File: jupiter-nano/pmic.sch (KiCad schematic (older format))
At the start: 51 parts, among them Q1 BSS138, Q2 BSS138, Q3 BSS138, Q4 BSS138, Q5 BSS138, U2 ACT8945AQJ305-T

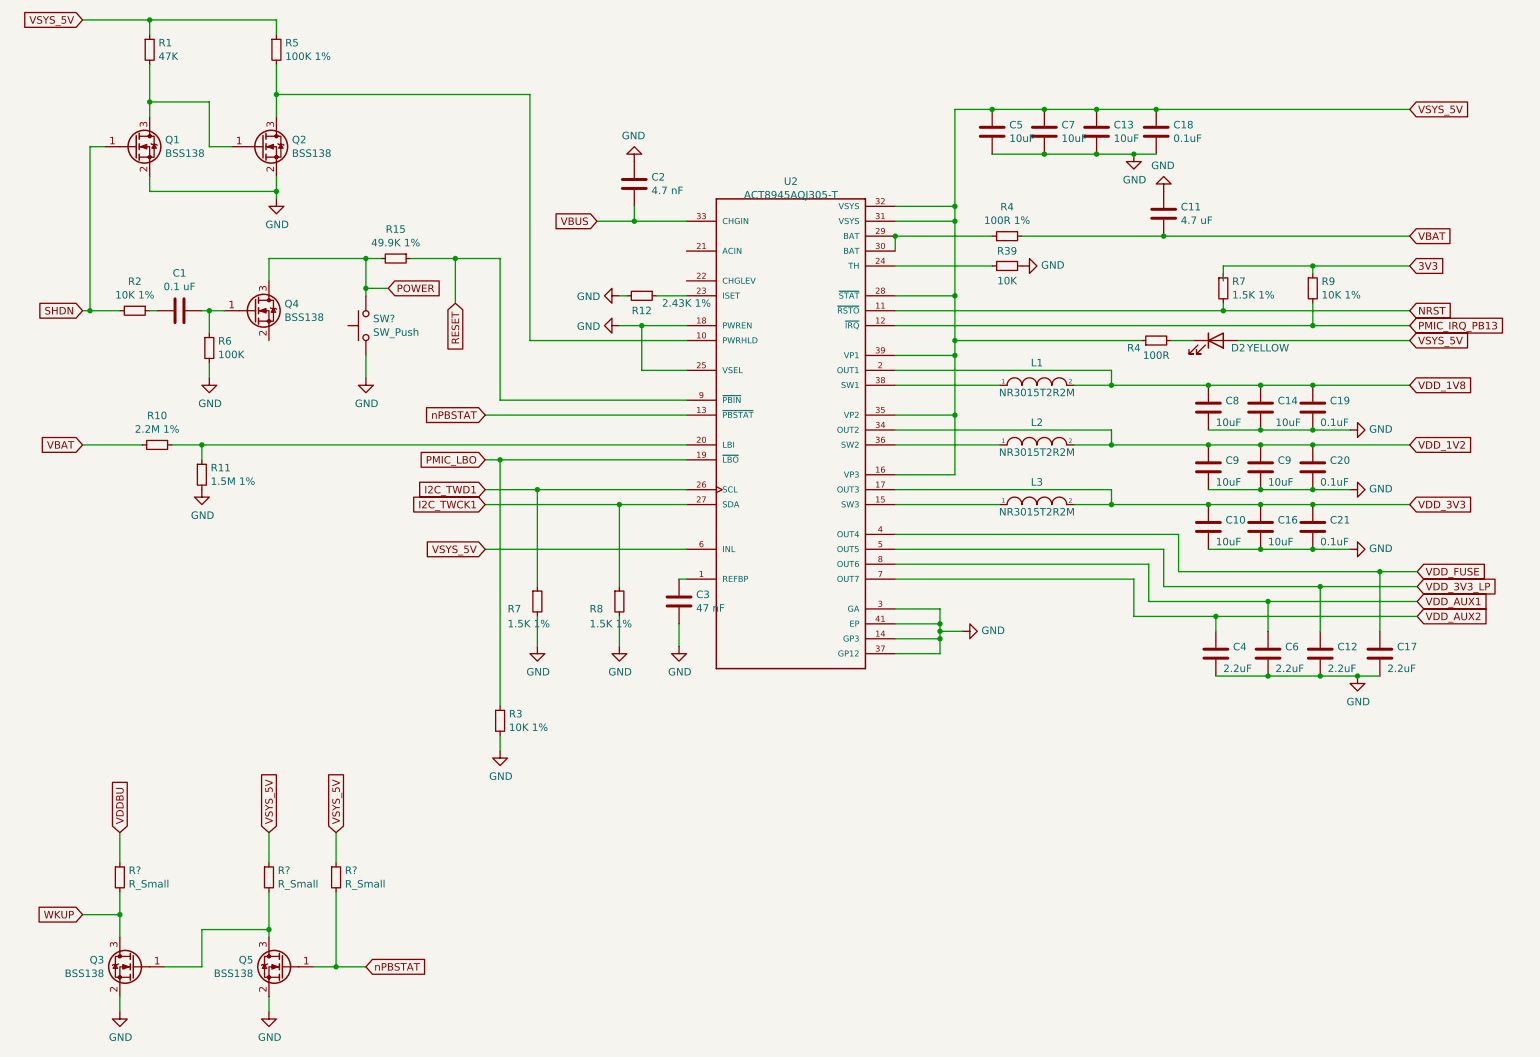
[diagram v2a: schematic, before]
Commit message: fixed error with INL
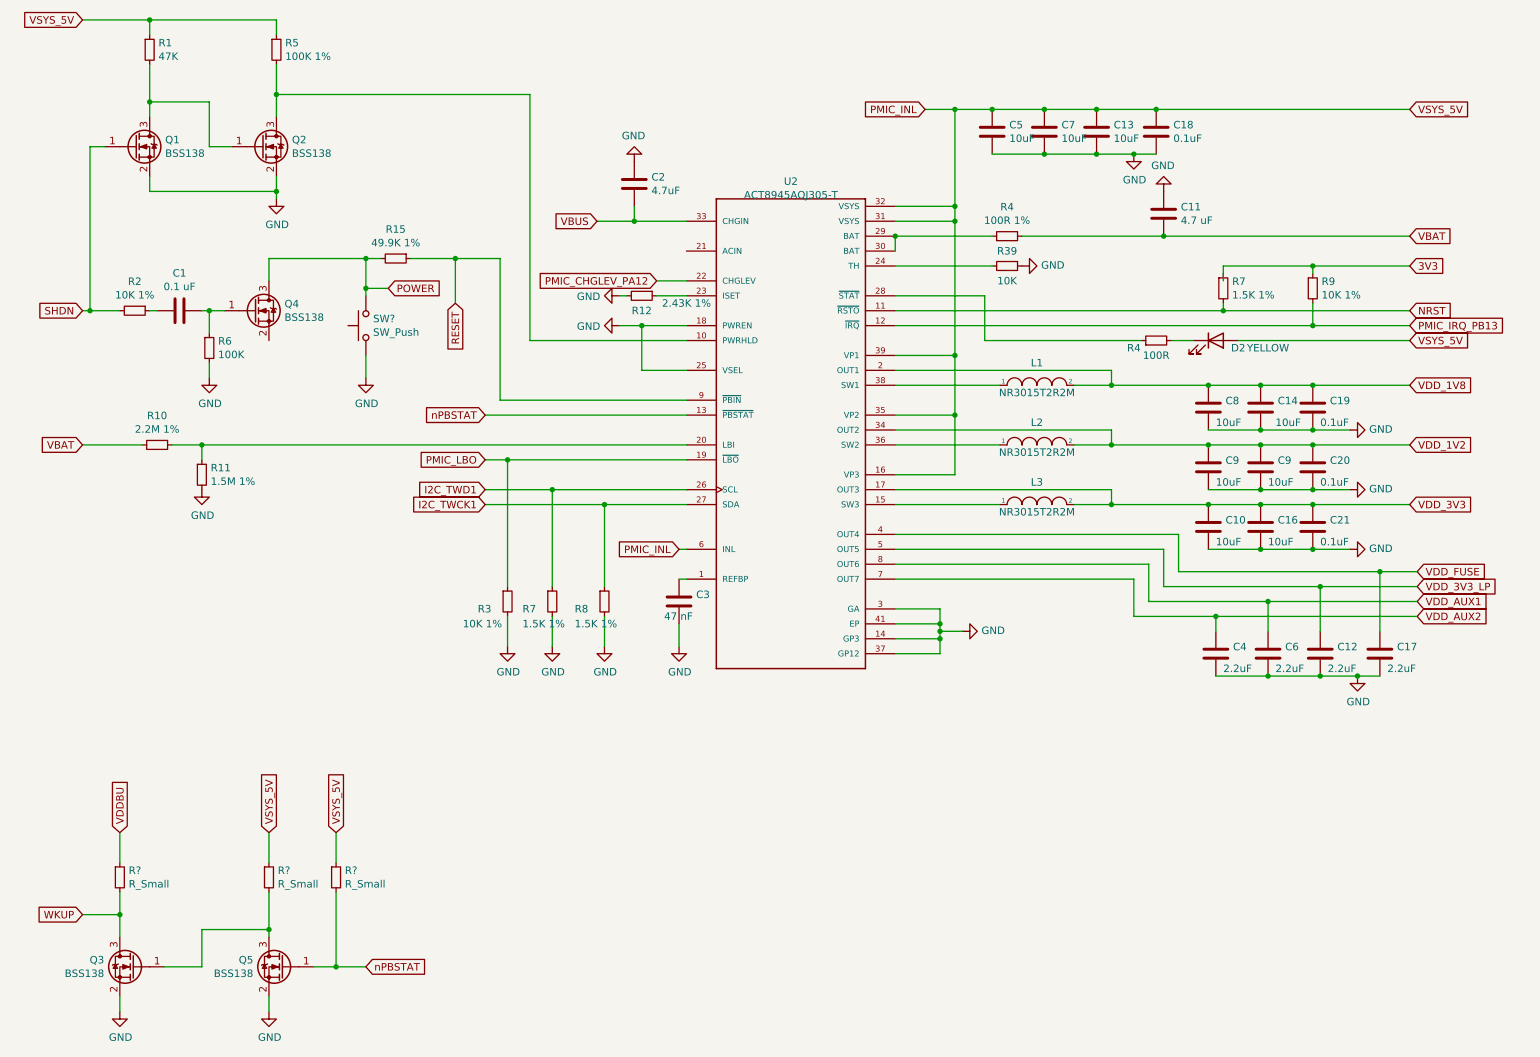
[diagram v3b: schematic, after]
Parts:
- C2: value 4.7 nF -> 4.7uF
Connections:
- net PMIC_CHGLEV_PA12: now reaches U2.22 (CHGLEV)
- net VSYS_5V renamed PMIC_INL
- net PMIC_INL: no longer R4.1, U2.28 (~STAT~)
- new net: R4.1, U2.28 (~STAT~)
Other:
- moved on the sheet: R3, R7, R8
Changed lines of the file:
@@
 P 4650 1900
 F 0 "C2" H 4765 1946 50  0000 L CNN
-F 1 "4.7 nF" H 4765 1855 50  0000 L CNN
+F 1 "4.7uF" H 4765 1855 50  0000 L CNN
 F 2 "Capacitor_SMD:C_0201_0603Metric" H 4688 1750 50  0001 C CNN
 F 3 "~" H 4650 1900 50  0001 C CNN
@@
 $EndComp
 Wire Wire Line
-	5000 3750 3750 3750
+	5000 3750 3800 3750
 Text GLabel 3650 3750 0    50   Input ~ 0
 PMIC_LBO
@@
 Text GLabel 9850 1400 2    50   Input ~ 0
 VSYS_5V
-Wire Wire Line
-	5000 4350 3650 4350
-Text GLabel 3650 4350 0    50   Input ~ 0
-VSYS_5V
+Text GLabel 4950 4350 0    50   Input ~ 0
+PMIC_INL
 $Comp
 L Device:C C5
@@
 $EndComp
 Wire Wire Line
-	6400 2650 6800 2650
-Wire Wire Line
-	6800 2650 6800 2150
-Wire Wire Line
 	6400 2450 7050 2450
 $Comp
@@
 Wire Wire Line
 	6800 3450 6800 3050
-Connection ~ 6800 2650
 Connection ~ 6800 3050
 Wire Wire Line
-	6800 3050 6800 2950
-Wire Wire Line
 	6400 3050 6800 3050
-Connection ~ 6800 2950
-Wire Wire Line
-	6800 2950 6800 2650
 Connection ~ 8200 2250
 Wire Wire Line
@@
 	8700 2950 9850 2950
 Wire Wire Line
-	6800 2950 8050 2950
-Wire Wire Line
 	6400 4750 6700 4750
 Wire Wire Line
@@
 P 4950 4700
 F 0 "C3" H 5065 4746 50  0000 L CNN
-F 1 "47 nF" H 5065 4655 50  0000 L CNN
+F 1 "47 nF" H 4850 4600 50  0000 L CNN
 F 2 "Capacitor_SMD:C_0201_0603Metric" H 4988 4550 50  0001 C CNN
 F 3 "~" H 4950 4700 50  0001 C CNN
@@
 nPBSTAT
 Wire Wire Line
-	5000 3950 4000 3950
-Text GLabel 3650 3950 0    50   Input ~ 0
-I2C_TWD1
-Wire Wire Line
-	5000 4050 4550 4050
+	5000 3950 4100 3950
+Wire Wire Line
+	5000 4050 4450 4050
 Text GLabel 3650 4050 0    50   Input ~ 0
 I2C_TWCK1
 Wire Wire Line
-	4000 3950 4000 4600
-Connection ~ 4000 3950
-Wire Wire Line
-	4000 3950 3650 3950
-Wire Wire Line
-	4550 4050 4550 4600
-Connection ~ 4550 4050
-Wire Wire Line
-	4550 4050 3650 4050
+	4100 3950 4100 4600
+Connection ~ 4100 3950
+Wire Wire Line
+	4100 3950 3650 3950
+Wire Wire Line
+	4450 4050 4450 4600
+Connection ~ 4450 4050
+Wire Wire Line
+	4450 4050 3650 4050
 $Comp
 L Device:R_Small R7
 U 1 1 5F5D8A0F
-P 4000 4700
-F 0 "R7" H 3800 4650 50  0000 L CNN
-F 1 "1.5K 1%" H 3800 4550 50  0000 L CNN
-F 2 "Capacitor_SMD:C_0201_0603Metric" H 4000 4700 50  0001 C CNN
-F 3 "~" H 4000 4700 50  0001 C CNN
-	1    4000 4700
+P 4100 4700
+F 0 "R7" H 3900 4650 50  0000 L CNN
+F 1 "1.5K 1%" H 3900 4550 50  0000 L CNN
+F 2 "Capacitor_SMD:C_0201_0603Metric" H 4100 4700 50  0001 C CNN
+F 3 "~" H 4100 4700 50  0001 C CNN
+	1    4100 4700
 	1    0    0    -1
 $EndComp
@@
 L Device:R_Small R8
 U 1 1 5F5D9763
-P 4550 4700
-F 0 "R8" H 4350 4650 50  0000 L CNN
-F 1 "1.5K 1%" H 4350 4550 50  0000 L CNN
-F 2 "Capacitor_SMD:C_0201_0603Metric" H 4550 4700 50  0001 C CNN
-F 3 "~" H 4550 4700 50  0001 C CNN
-	1    4550 4700
-	1    0    0    -1
-$EndComp
-Wire Wire Line
-	4000 4800 4000 5000
-Wire Wire Line
-	4550 4800 4550 5000
+P 4450 4700
+F 0 "R8" H 4250 4650 50  0000 L CNN
+F 1 "1.5K 1%" H 4250 4550 50  0000 L CNN
+F 2 "Capacitor_SMD:C_0201_0603Metric" H 4450 4700 50  0001 C CNN
+F 3 "~" H 4450 4700 50  0001 C CNN
+	1    4450 4700
+	1    0    0    -1
+$EndComp
+Wire Wire Line
+	4100 4800 4100 5000
+Wire Wire Line
+	4450 4800 4450 5000
 $Comp
 L power:GND #PWR?
 U 1 1 5F5E58C5
-P 4000 5000
-F 0 "#PWR?" H 4000 4750 50  0001 C CNN
-F 1 "GND" H 4005 4827 50  0000 C CNN
-F 2 "" H 4000 5000 50  0001 C CNN
-F 3 "" H 4000 5000 50  0001 C CNN
-	1    4000 5000
+P 4100 5000
+F 0 "#PWR?" H 4100 4750 50  0001 C CNN
+F 1 "GND" H 4105 4827 50  0000 C CNN
+F 2 "" H 4100 5000 50  0001 C CNN
+F 3 "" H 4100 5000 50  0001 C CNN
+	1    4100 5000
 	1    0    0    -1
 $EndComp
@@
 L power:GND #PWR?
 U 1 1 5F5E6EDB
-P 4550 5000
-F 0 "#PWR?" H 4550 4750 50  0001 C CNN
-F 1 "GND" H 4555 4827 50  0000 C CNN
-F 2 "" H 4550 5000 50  0001 C CNN
-F 3 "" H 4550 5000 50  0001 C CNN
-	1    4550 5000
-	1    0    0    -1
-$EndComp
-Wire Wire Line
-	3750 3750 3750 5400
-Connection ~ 3750 3750
-Wire Wire Line
-	3750 3750 3650 3750
+P 4450 5000
+F 0 "#PWR?" H 4450 4750 50  0001 C CNN
+F 1 "GND" H 4455 4827 50  0000 C CNN
+F 2 "" H 4450 5000 50  0001 C CNN
+F 3 "" H 4450 5000 50  0001 C CNN
+	1    4450 5000
+	1    0    0    -1
+$EndComp
+Wire Wire Line
+	3800 3750 3800 4600
+Connection ~ 3800 3750
+Wire Wire Line
+	3800 3750 3650 3750
 $Comp
 L Device:R_Small R3
 U 1 1 5F6066C1
-P 3750 5500
-F 0 "R3" H 3809 5546 50  0000 L CNN
-F 1 "10K 1%" H 3809 5455 50  0000 L CNN
-F 2 "" H 3750 5500 50  0001 C CNN
-F 3 "~" H 3750 5500 50  0001 C CNN
-	1    3750 5500
-	1    0    0    -1
-$EndComp
-Wire Wire Line
-	3750 5600 3750 5700
+P 3800 4700
+F 0 "R3" H 3600 4650 50  0000 L CNN
+F 1 "10K 1%" H 3500 4550 50  0000 L CNN
+F 2 "" H 3800 4700 50  0001 C CNN
+F 3 "~" H 3800 4700 50  0001 C CNN
+	1    3800 4700
+	1    0    0    -1
+$EndComp
+Wire Wire Line
+	3800 4800 3800 5000
 $Comp
 L power:GND #PWR?
 U 1 1 5F60CEF0
-P 3750 5700
-F 0 "#PWR?" H 3750 5450 50  0001 C CNN
-F 1 "GND" H 3755 5527 50  0000 C CNN
-F 2 "" H 3750 5700 50  0001 C CNN
-F 3 "" H 3750 5700 50  0001 C CNN
-	1    3750 5700
+P 3800 5000
+F 0 "#PWR?" H 3800 4750 50  0001 C CNN
+F 1 "GND" H 3805 4827 50  0000 C CNN
+F 2 "" H 3800 5000 50  0001 C CNN
+F 3 "" H 3800 5000 50  0001 C CNN
+	1    3800 5000
 	1    0    0    -1
 $EndComp
@@
 Wire Wire Line
 	2250 1300 3950 1300
+Wire Wire Line
+	6800 2150 6800 3050
+Wire Wire Line
+	6400 2650 7000 2650
+Wire Wire Line
+	7000 2650 7000 2950
+Wire Wire Line
+	7000 2950 8050 2950
+Wire Wire Line
+	5000 2550 4800 2550
+Text GLabel 4800 2550 0    50   Input ~ 0
+PMIC_CHGLEV_PA12
+Wire Wire Line
+	5000 4350 4950 4350
+Wire Wire Line
+	6800 1400 6600 1400
+Connection ~ 6800 1400
+Text GLabel 6600 1400 0    50   Input ~ 0
+PMIC_INL
+Text GLabel 3650 3950 0    50   Input ~ 0
+I2C_TWD1
 $EndSCHEMATC

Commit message: WIP clocking done
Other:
- moved on the sheet: Q3, Q5, R?
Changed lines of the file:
@@
 L Transistor_FET:BSS138 Q3
 U 1 1 5F66BE91
-P 1300 7150
-F 0 "Q3" H 1505 7196 50  0000 L CNN
-F 1 "BSS138" H 1505 7105 50  0000 L CNN
-F 2 "Package_TO_SOT_SMD:SOT-23" H 1500 7075 50  0001 L CIN
-F 3 "https://www.fairchildsemi.com/datasheets/BS/BSS138.pdf" H 1300 7150 50  0001 L CNN
-	1    1300 7150
+P 2300 6900
+F 0 "Q3" H 2505 6946 50  0000 L CNN
+F 1 "BSS138" H 2505 6855 50  0000 L CNN
+F 2 "Package_TO_SOT_SMD:SOT-23" H 2500 6825 50  0001 L CIN
+F 3 "https://www.fairchildsemi.com/datasheets/BS/BSS138.pdf" H 2300 6900 50  0001 L CNN
+	1    2300 6900
 	-1   0    0    -1
 $EndComp
@@
 L Transistor_FET:BSS138 Q5
 U 1 1 5F684C12
-P 2300 7150
-F 0 "Q5" H 2505 7196 50  0000 L CNN
-F 1 "BSS138" H 2505 7105 50  0000 L CNN
-F 2 "Package_TO_SOT_SMD:SOT-23" H 2500 7075 50  0001 L CIN
-F 3 "https://www.fairchildsemi.com/datasheets/BS/BSS138.pdf" H 2300 7150 50  0001 L CNN
-	1    2300 7150
+P 3300 6900
+F 0 "Q5" H 3505 6946 50  0000 L CNN
+F 1 "BSS138" H 3505 6855 50  0000 L CNN
+F 2 "Package_TO_SOT_SMD:SOT-23" H 3500 6825 50  0001 L CIN
+F 3 "https://www.fairchildsemi.com/datasheets/BS/BSS138.pdf" H 3300 6900 50  0001 L CNN
+	1    3300 6900
 	-1   0    0    -1
 $EndComp
 Wire Wire Line
-	2200 6950 2200 6900
+	3200 6700 3200 6650
 Wire Wire Line
-	2200 6900 1750 6900
+	3200 6650 2750 6650
 Wire Wire Line
-	1750 6900 1750 7150
+	2750 6650 2750 6900
 Wire Wire Line
-	1750 7150 1500 7150
+	2750 6900 2500 6900
 Wire Wire Line
-	2200 7350 2200 7450
+	3200 7100 3200 7200
 Wire Wire Line
-	1200 7350 1200 7450
+	2200 7100 2200 7200
 $Comp
 L power:GND #PWR?
 U 1 1 5F6CBF6E
-P 1200 7450
-F 0 "#PWR?" H 1200 7200 50  0001 C CNN
-F 1 "GND" H 1205 7277 50  0000 C CNN
-F 2 "" H 1200 7450 50  0001 C CNN
-F 3 "" H 1200 7450 50  0001 C CNN
-	1    1200 7450
+P 2200 7200
+F 0 "#PWR?" H 2200 6950 50  0001 C CNN
+F 1 "GND" H 2205 7027 50  0000 C CNN
+F 2 "" H 2200 7200 50  0001 C CNN
+F 3 "" H 2200 7200 50  0001 C CNN
+	1    2200 7200
 	1    0    0    -1
 $EndComp
@@
 L power:GND #PWR?
 U 1 1 5F6CCAD6
-P 2200 7450
-F 0 "#PWR?" H 2200 7200 50  0001 C CNN
-F 1 "GND" H 2205 7277 50  0000 C CNN
-F 2 "" H 2200 7450 50  0001 C CNN
-F 3 "" H 2200 7450 50  0001 C CNN
-	1    2200 7450
+P 3200 7200
+F 0 "#PWR?" H 3200 6950 50  0001 C CNN
+F 1 "GND" H 3205 7027 50  0000 C CNN
+F 2 "" H 3200 7200 50  0001 C CNN
+F 3 "" H 3200 7200 50  0001 C CNN
+	1    3200 7200
 	1    0    0    -1
 $EndComp
 Wire Wire Line
-	2500 7150 2650 7150
-Text GLabel 2850 7150 2    50   Input ~ 0
+	3500 6900 3650 6900
+Text GLabel 3850 6900 2    50   Input ~ 0
 nPBSTAT
 Wire Wire Line
-	2200 6900 2200 6650
-Connection ~ 2200 6900
+	3200 6650 3200 6400
+Connection ~ 3200 6650
 Wire Wire Line
-	2650 7150 2650 6650
-Connection ~ 2650 7150
+	3650 6900 3650 6400
+Connection ~ 3650 6900
 Wire Wire Line
-	2650 7150 2850 7150
+	3650 6900 3850 6900
 Wire Wire Line
-	1200 6950 1200 6800
-Text GLabel 2650 6250 1    50   Input ~ 0
+	2200 6700 2200 6550
+Text GLabel 3650 6000 1    50   Input ~ 0
 VSYS_5V
-Text GLabel 2200 6250 1    50   Input ~ 0
+Text GLabel 3200 6000 1    50   Input ~ 0
 VSYS_5V
-Text GLabel 1200 6250 1    50   Input ~ 0
+Text GLabel 2200 6000 1    50   Input ~ 0
 VDDBU
 $Comp
 L Device:R_Small R?
 U 1 1 5F7027C3
-P 2650 6550
-F 0 "R?" H 2709 6596 50  0000 L CNN
-F 1 "R_Small" H 2709 6505 50  0000 L CNN
-F 2 "" H 2650 6550 50  0001 C CNN
-F 3 "~" H 2650 6550 50  0001 C CNN
-	1    2650 6550
+P 3650 6300
+F 0 "R?" H 3709 6346 50  0000 L CNN
+F 1 "R_Small" H 3709 6255 50  0000 L CNN
+F 2 "" H 3650 6300 50  0001 C CNN
+F 3 "~" H 3650 6300 50  0001 C CNN
+	1    3650 6300
 	1    0    0    -1
 $EndComp
@@
 L Device:R_Small R?
 U 1 1 5F70325F
-P 2200 6550
-F 0 "R?" H 2259 6596 50  0000 L CNN
-F 1 "R_Small" H 2259 6505 50  0000 L CNN
-F 2 "" H 2200 6550 50  0001 C CNN
-F 3 "~" H 2200 6550 50  0001 C CNN
-	1    2200 6550
+P 3200 6300
+F 0 "R?" H 3259 6346 50  0000 L CNN
+F 1 "R_Small" H 3259 6255 50  0000 L CNN
+F 2 "" H 3200 6300 50  0001 C CNN
+F 3 "~" H 3200 6300 50  0001 C CNN
+	1    3200 6300
 	1    0    0    -1
 $EndComp
@@
 L Device:R_Small R?
 U 1 1 5F703D5F
-P 1200 6550
-F 0 "R?" H 1259 6596 50  0000 L CNN
-F 1 "R_Small" H 1259 6505 50  0000 L CNN
-F 2 "" H 1200 6550 50  0001 C CNN
-F 3 "~" H 1200 6550 50  0001 C CNN
-	1    1200 6550
+P 2200 6300
+F 0 "R?" H 2259 6346 50  0000 L CNN
+F 1 "R_Small" H 2259 6255 50  0000 L CNN
+F 2 "" H 2200 6300 50  0001 C CNN
+F 3 "~" H 2200 6300 50  0001 C CNN
+	1    2200 6300
 	1    0    0    -1
 $EndComp
-Connection ~ 1200 6800
+Connection ~ 2200 6550
 Wire Wire Line
-	1200 6800 1200 6650
+	2200 6550 2200 6400
 Wire Wire Line
-	1200 6250 1200 6450
+	2200 6000 2200 6200
 Wire Wire Line
-	2200 6250 2200 6450
+	3200 6000 3200 6200
 Wire Wire Line
-	2650 6250 2650 6450
+	3650 6000 3650 6200
 Wire Wire Line
-	950  6800 1200 6800
-Text GLabel 950  6800 0    50   Input ~ 0
+	1950 6550 2200 6550
+Text GLabel 1950 6550 0    50   Input ~ 0
 WKUP
 $Comp

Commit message: cleanup
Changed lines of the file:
@@
 U 1 1 5F54B6F8
 P 5700 3550
-F 0 "U2" H 5700 5217 50  0000 C CNN
-F 1 "ACT8945AQJ305-T" H 5700 5126 50  0000 C CNN
+F 0 "U2" H 5700 5350 50  0000 C CNN
+F 1 "ACT8945AQJ305-T" H 5700 5200 50  0000 C CNN
 F 2 "QFN40P500X500X80-41N" H 5700 3550 50  0001 L BNN
 F 3 "None" H 5700 3550 50  0001 L BNN
